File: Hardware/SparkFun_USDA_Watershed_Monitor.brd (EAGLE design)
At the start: 63.5 x 63.5 mm, 186 parts, among them J10 QWIIC_RIGHT_ANGLE, J3 QWIIC_RIGHT_ANGLE, J4 U.FL, J5 RJ45, J7 RJ45, J8 RJ45, J9 RJ45, Q1 20V/4.2A/52mΩ/1.4W, Q2 20V/0.2A/8MHz/1.2Ω/1Vth, Q3 20V/0.2A/8MHz/1.2Ω/1Vth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

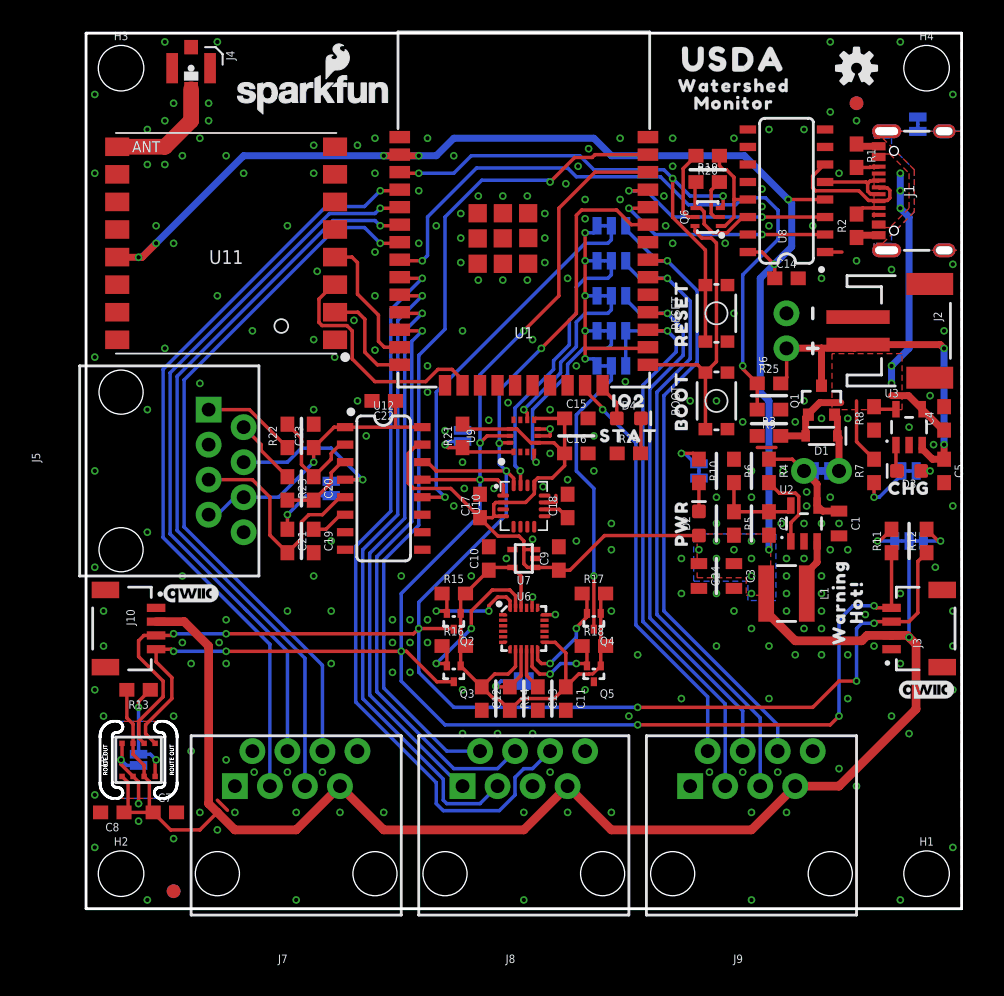
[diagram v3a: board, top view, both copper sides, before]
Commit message: Replace center RJ45 with header pins
Fully populate other RJ45's with GPIO pins, leaving 2 free GPIO pins going to header pins
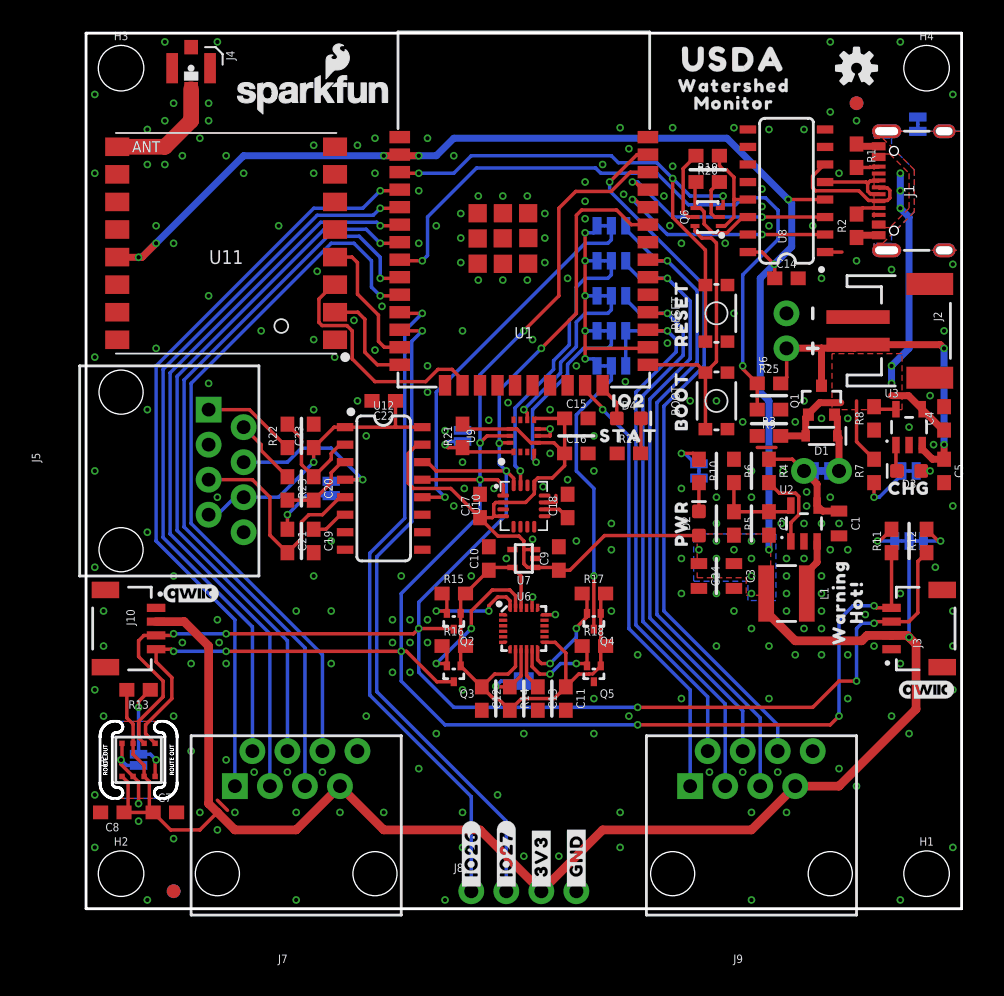
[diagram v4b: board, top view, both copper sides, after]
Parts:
- removed U$56: (no value), output:NC0
- added U$53: (no value), output:#_GND#0
- J8: value RJ45 -> (none); device SparkFun-Connectors:RJ45-8 -> SparkFun-Connectors:1X04_NO_SILK
- U$47: device output:NC0 -> output:#_IO26#0
- U$48: device output:NC0 -> output:#_IO27#0
- U$49: device output:IO270 -> output:#_3V3#0
- U$50: device output:IO260 -> output:#_GND#0
- U$51: device output:NC0 -> output:#_3V3#0
- U$6: device output:GND0 -> output:#_IO26#0
- U$7: device output:3V30 -> output:#_IO27#0
- moved U$52 20.3 mm to (13.3, 4.57)
- moved U$48 17.8 mm to (30.5, 1.27), turned to 90 degrees
- moved U$32 17.7 mm to (33.7, 12.4)
- moved U$36 17.7 mm to (33.7, 9.40)
- moved U$38 17.7 mm to (33.7, 7.87)
- moved U$33 17.7 mm to (29.8, 12.4)
- moved U$34 17.7 mm to (33.7, 10.9)
- moved U$37 17.7 mm to (29.8, 9.40)
- moved U$39 17.7 mm to (29.8, 7.87)
- moved U$45 17.7 mm to (31.8, 14.0)
- moved U$35 17.7 mm to (29.8, 10.9)
- moved U$78 16.6 mm to (46.4, 4.57)
- moved U$54 12.8 mm to (17.1, 3.05)
- moved U$47 11.8 mm to (27.9, 1.27), turned to 90 degrees
- moved U$50 5.19 mm to (35.6, 1.27), flipped to the top, turned to 90 degrees
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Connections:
- net 3.3V: now also J8.3; no longer J8.7
- net ESP_I34: now also J7.3; no longer J7.5
- net ESP_I35: now also J7.4; no longer J7.6
- net ESP_I36: now also J7.1; no longer J7.3
- net ESP_I39: now also J7.2; no longer J7.4
- net ESP_IO15: now also J9.1; no longer J9.2
- net ESP_IO16: now also J9.2; no longer J9.3
- net ESP_IO17: now also J9.3; no longer J9.4
- net ESP_IO18: now also J9.4; no longer J9.5
- net ESP_IO19: now also J9.5; no longer J9.6
- net ESP_IO23: now also J9.6; no longer J8.2
- net ESP_IO25: now also J7.6; no longer J8.3
- net ESP_IO27: now also J8.2; no longer J8.4
- net ESP_IO33: now also J7.5; no longer J8.6
- net GND: now also J8.4; no longer J8.8
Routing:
- net ESP_IO23: track 61.6 -> 52.3 mm
- net ESP_IO26: track 40.4 -> 48.2 mm
- net ESP_IO25: track 47.0 -> 52.7 mm
- net ESP_IO27: track 42.1 -> 47.6 mm
- net ESP_IO18: track 46.8 -> 44.1 mm
- net ESP_IO16: track 43.8 -> 41.1 mm
- net ESP_IO19: track 46.5 -> 49.0 mm
- net ESP_IO17: track 41.2 -> 43.6 mm
- net ESP_IO15: track 30.2 -> 32.2 mm
- net 3.3V: track 267.0 -> 268.1 mm
- net GND: vias 245 -> 252

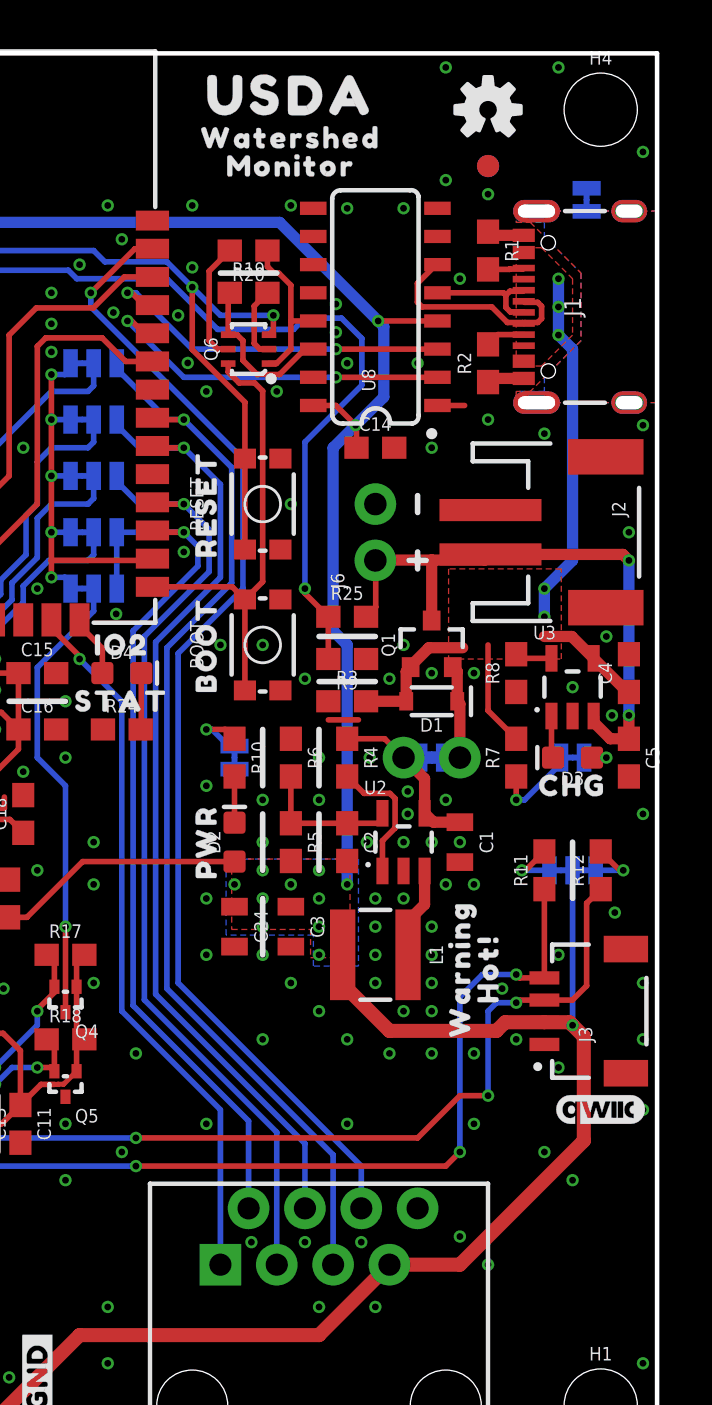
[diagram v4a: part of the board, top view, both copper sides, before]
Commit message: Add 5V header
Add 5V header for power injection
Rename V_USB  net to 5V
Add diode to USB input to protect against 5V contention
Header  took place of I2C pullups, so those got moved to other side of Qwiic connector
Add units to measures
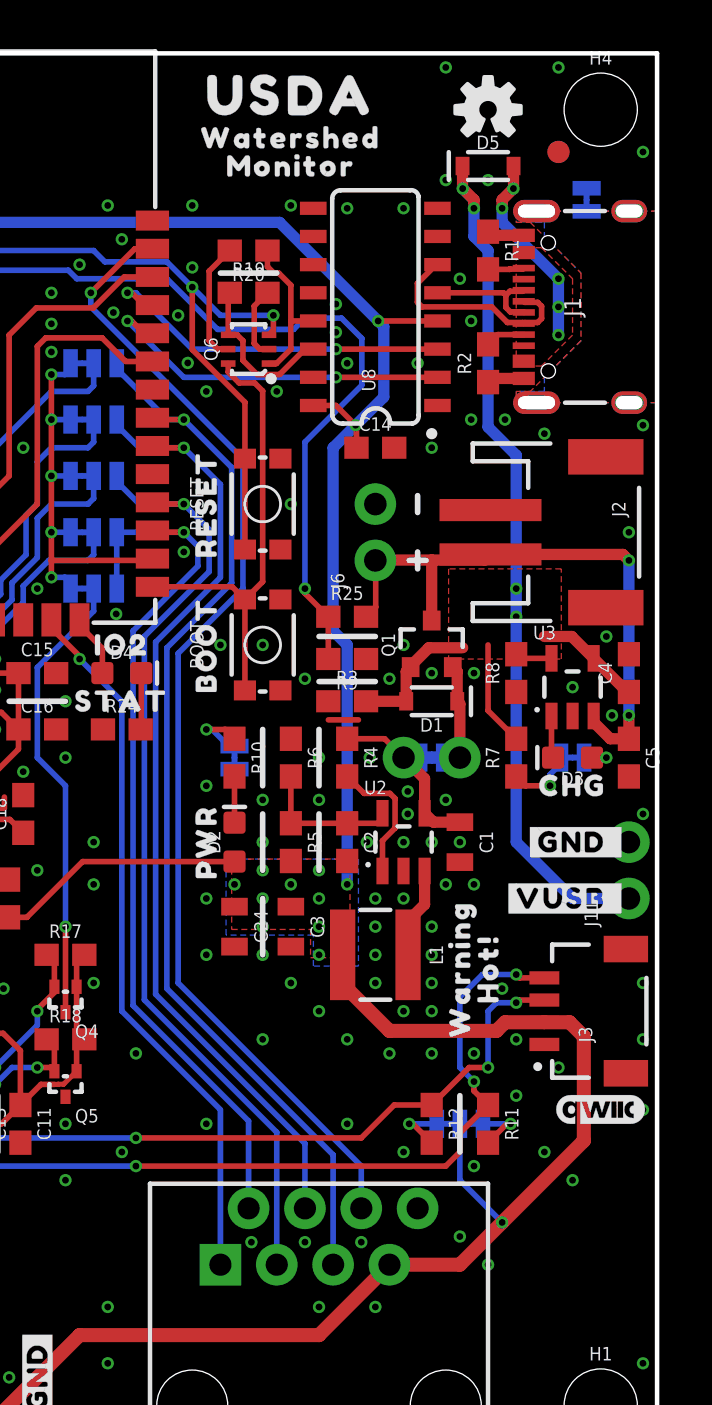
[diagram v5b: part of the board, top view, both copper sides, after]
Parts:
- added D5: 3A/10V/280mV, SparkFun-DiscreteSemi:SOD-323
- added J11: (no value), SparkFun-Connectors:1X02_NO_SILK
- added U$56: (no value), output:#VUSB_#0
- added U$79: (no value), output:#GND_#0
- added U$80: (no value), output:#_GND#0
- added U$81: (no value), output:#_VUSB#4
- moved R12 13.7 mm to (53.3, 15.2), turned to 270 degrees
- moved U$15 12.5 mm to (54.6, 16.9)
- moved I2C 12.5 mm to (54.6, 15.2), turned to 180 degrees
- moved R11 11.7 mm to (55.9, 15.2), turned to 270 degrees
- moved FD3 3.24 mm to (59.1, 59.1)
- moved FD4 3.24 mm to (59.1, 59.1)
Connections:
- new net 5V: C4.1, D1.A, D5.C, J11.1, Q1.1, R3.2, R7.2, U3.4
- net GND: now also J11.2
- net V_USB: now also D5.A; no longer C4.1, D1.A, Q1.1, R3.2, R7.2, U3.4
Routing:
- net 5V: track 0.00 -> 54.5 mm, vias 0 -> 4
- net V_USB: track 31.8 -> 9.98 mm
- net SDA: track 131.7 -> 124.2 mm
- net SCL: track 135.3 -> 132.3 mm
- net 3.3V: track 268.1 -> 266.3 mm
- net GND: track 18.6 -> 17.4 mm, vias 252 -> 254
- net N$10: track 4.02 -> 3.17 mm
- added copper zone on layer 1, net 5V
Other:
- board text added: "Units: inches"

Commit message: Schematic review updates
Add note about ICM-20948 going EOL
Add I2C addresses of all sensors
Add max input voltage to regulators
Add value to 3V3 regulator
Add boot table to auto reset
Change power LED resistor to 1k
Move load cell connector with other connectors
Remove bar from interrupt net names
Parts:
- R10: value 2.2k -> 1k
- U2: value (none) -> AP3429A
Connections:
- net !ICM_INT! renamed ICM_INT
- net !ISM_INT1! renamed ISM_INT1
- net !ISM_INT2! renamed ISM_INT2
- net !MMC_INT! renamed MMC_INT
- net !NAU_INT! renamed NAU_INT
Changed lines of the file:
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@@
 <drawing>
 <settings>
-<setting alwaysvectorfont="yes"/>
+<setting alwaysvectorfont="no"/>
 <setting verticaltext="up"/>
 </settings>
@@
 <attribute name="VALUE" x="56.642" y="49.53" size="0.6096" layer="27" font="vector" ratio="20" rot="R90" align="top-center"/>
 </element>
-<element name="U2" library="SparkFun-IC-Power" package="SOT23-5" value="" x="52.07" y="27.94" smashed="yes">
+<element name="U2" library="SparkFun-IC-Power" package="SOT23-5" value="AP3429A" x="52.07" y="27.94" smashed="yes">
 <attribute name="NAME" x="50.292" y="30.099" size="0.6096" layer="25" ratio="20"/>
 <attribute name="PROD_ID" value="IC-14465" x="52.07" y="27.94" size="1.778" layer="27" font="vector" ratio="15" display="off"/>
@@
 <attribute name="VALUE" x="57.912" y="35.56" size="0.6096" layer="27" font="vector" ratio="20" rot="R90" align="top-center"/>
 </element>
-<element name="R10" library="SparkFun-Resistors" package="0603" value="2.2k" x="44.45" y="31.75" smashed="yes" rot="R270">
+<element name="R10" library="SparkFun-Resistors" package="0603" value="1k" x="44.45" y="31.75" smashed="yes" rot="R270">
 <attribute name="NAME" x="45.212" y="31.75" size="0.6096" layer="25" font="vector" ratio="20" rot="R270" align="bottom-center"/>
-<attribute name="PROD_ID" value="RES-08272" x="44.45" y="31.75" size="1.778" layer="27" font="vector" ratio="15" rot="R270" display="off"/>
-<attribute name="VALUE" x="43.688" y="31.75" size="0.6096" layer="27" font="vector" ratio="20" rot="R270" align="top-center"/>
+<attribute name="PROD_ID" value="RES-07856" x="44.45" y="31.75" size="1.778" layer="27" font="vector" ratio="15" rot="R270" display="off"/>
+<attribute name="VALUE" value="1k" x="43.688" y="31.75" size="0.6096" layer="27" font="vector" ratio="20" rot="R270" align="top-center"/>
 </element>
 <element name="PWR" library="SparkFun-Jumpers" package="SMT-JUMPER_2_NC_TRACE_SILK" package3d_urn="urn:adsk.eagle:package:39281/1" value="JUMPER-SMT_2_NC_TRACE_SILK" x="44.45" y="31.75" smashed="yes" rot="MR90">
@@
 <contactref element="Q5" pad="3"/>
 </signal>
-<signal name="!ICM_INT!">
+<signal name="ICM_INT">
 <contactref element="Q4" pad="3"/>
 <contactref element="ICM_INT" pad="2"/>
@@
 <wire x1="46.443" y1="53.594" x2="46.99" y2="53.047" width="0.254" layer="1"/>
 </signal>
-<signal name="!ISM_INT2!">
+<signal name="ISM_INT2">
 <contactref element="U9" pad="P9"/>
 <contactref element="ISM_INT2" pad="2"/>
@@
 <wire x1="35.56" y1="40.767" x2="35.56" y2="42.545" width="0.254" layer="16"/>
 </signal>
-<signal name="!ISM_INT1!">
+<signal name="ISM_INT1">
 <contactref element="U9" pad="P4"/>
 <contactref element="ISM_INT1" pad="2"/>
@@
 <wire x1="34.321" y1="28.964" x2="33.256" y2="28.964" width="0.254" layer="1"/>
 </signal>
-<signal name="!MMC_INT!">
+<signal name="MMC_INT">
 <contactref element="U10" pad="15"/>
 <contactref element="MMC_INT" pad="2"/>
@@
 <wire x1="18.454" y1="28.575" x2="18.79" y2="28.575" width="0.254" layer="1"/>
 </signal>
-<signal name="!NAU_INT!">
+<signal name="NAU_INT">
 <contactref element="U12" pad="12"/>
 <contactref element="NAU_INT" pad="2"/>

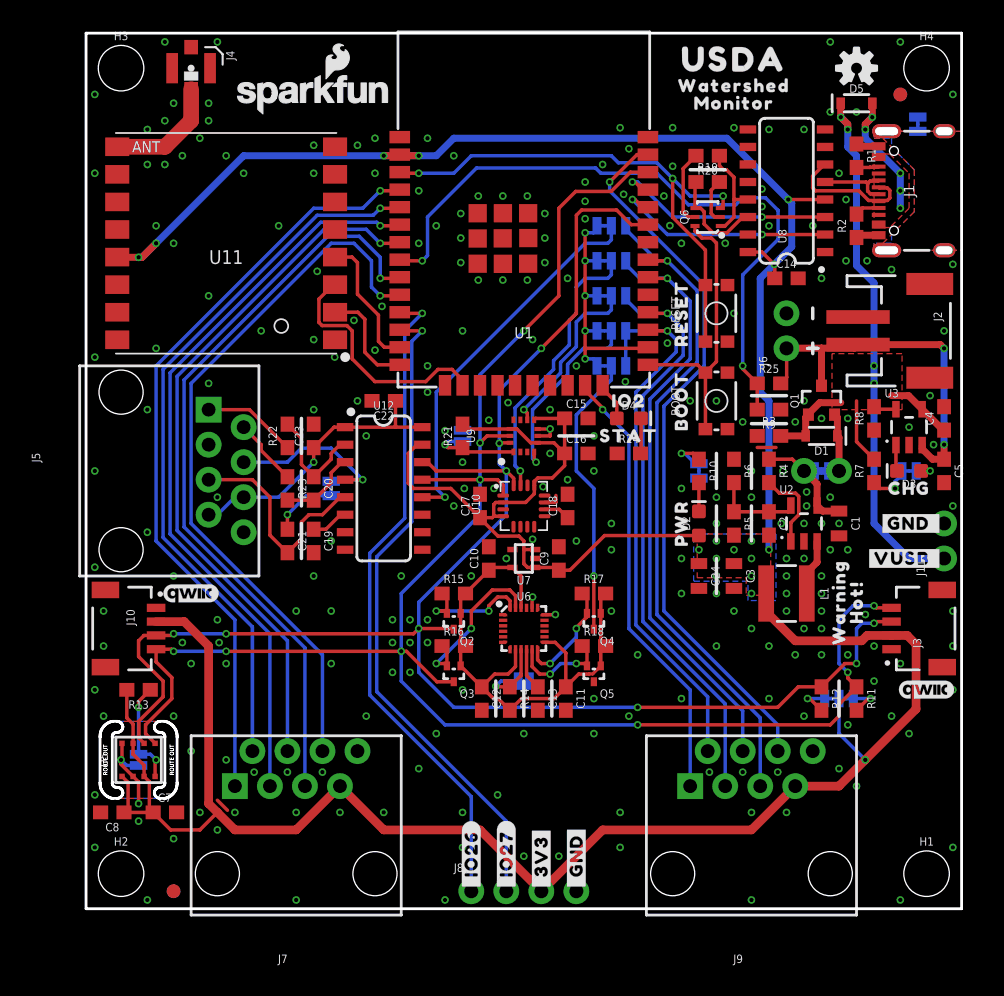
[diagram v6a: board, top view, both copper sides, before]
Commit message: Design review updates
Replace "VUSB" buzzard label with "5V"
Add test point for 1.8V net
Nudge C22 to the left
Add selective solder paths
Move u.FL connector away from board edge
Nudge GPIO lines under load cell connector to the left
Rename GPIO nets that aren't broken out to connectors with more helpful names
Fix CH340 capacitors (100nF on VCC only, add 10nF to V3 and disconnect from 3.3V net)
Move USB connector to not overhang edge (better for panelization)
Move CC resistors and VUSB diode next to battery PTH pads
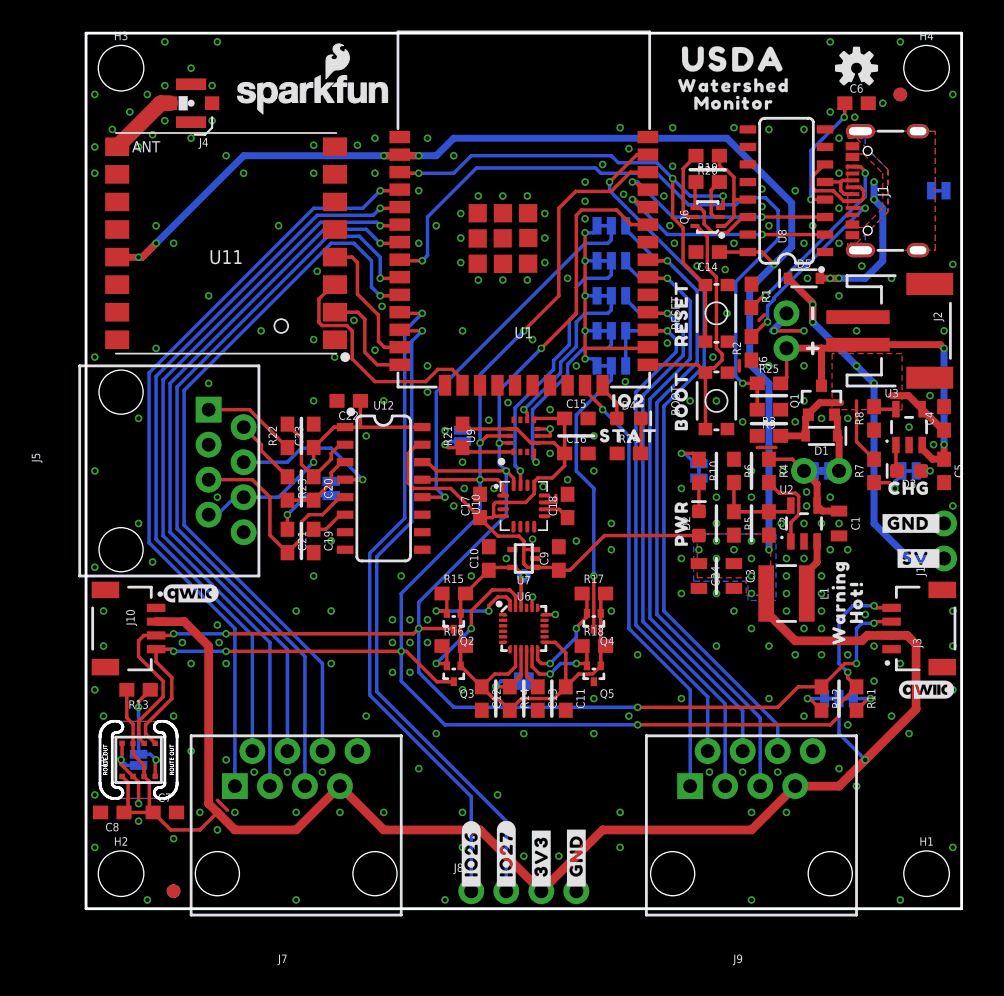
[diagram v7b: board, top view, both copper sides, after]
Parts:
- removed U$56: (no value), output:#VUSB_#0
- removed U$81: (no value), output:#_VUSB#4
- added C6: 10nF, SparkFun-Capacitors:0603
- added TP1: TEST-POINT3X4, SparkFun-Connectors:PAD.03X.04
- added U$82: (no value), output:#5V_#0
- added U$83: (no value), output:#_5V#6
- moved D5 13.3 mm to (52.1, 45.7)
- moved R1 12.7 mm to (48.3, 44.5)
- moved R2 11.7 mm to (48.3, 40.6)
- moved C14 6.02 mm to (45.1, 47.6), turned to 180 degrees
- moved SHLD 5.06 mm to (61.8, 52.1), turned to 0 degrees
- moved U$22 3.99 mm to (61.0, 52.1), turned to 180 degrees
- moved C22 2.54 mm to (19.1, 36.8)
- moved J4 2.54 mm to (7.62, 58.4), turned to 180 degrees
- moved J1 1.91 mm to (55.2, 52.1)
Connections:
- net !ICM_INT_1V8! renamed ICM_INT_1V8
- net ESP_IO0 renamed ESP_IO0_BOOT
- net ESP_IO2 renamed STAT
- net ESP_IO32 renamed V_BATT_2
- net ESP_IO4 renamed ESP_INT_COM
- new net N$12: C6.1, U8.4
- net 1.8V: now also TP1.1
- net 3.3V: no longer U8.4
- net GND: now also C6.2
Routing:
- net N$4: track 1.63 -> 14.5 mm, vias 0 -> 2
- net N$5: track 1.79 -> 13.8 mm, vias 0 -> 2
- net 5V: track 54.5 -> 43.5 mm
- net N$12: track 0.00 -> 9.02 mm, vias 0 -> 2
- net GND: track 17.4 -> 21.3 mm, vias 254 -> 270
- net N$25: track 8.43 -> 5.14 mm
- net USB_DN: track 9.65 -> 7.74 mm
- net USB_DP: track 5.48 -> 3.61 mm
- net V_USB: track 9.98 -> 11.7 mm, vias 5 -> 4
- net V_BATT_2: track 49.5 -> 50.6 mm
- net 3.3V: track 266.3 -> 265.3 mm, vias 17 -> 16
- net 1.8V: track 40.2 -> 40.4 mm, vias 0 -> 1
